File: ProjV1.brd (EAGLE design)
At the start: 94.9 x 63.5 mm, 24 parts, among them IC1 CD4007UBM, IC2 CD4007UBM, IC3 CD4007UBM, SW1 EC12E_SW, U1 MIC5504-3.3YM5-T5, U2 MCP2200-I/SS, U3 ATMEGA328PB-AU, Y1 12MHz

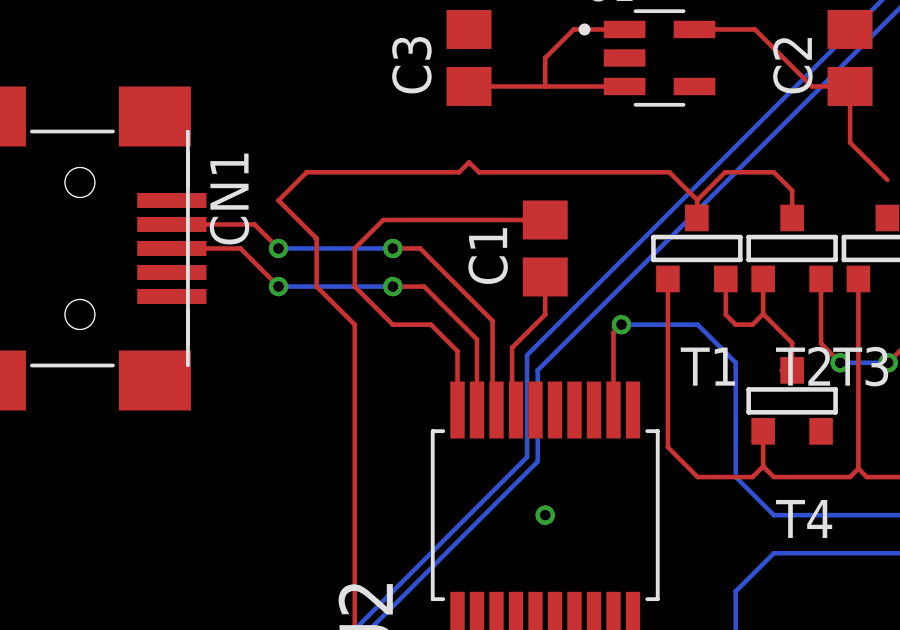
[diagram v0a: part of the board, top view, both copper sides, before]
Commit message: Updated schematic and pdf
Switched serial chip to run on 3.3V and  updated the pdf file
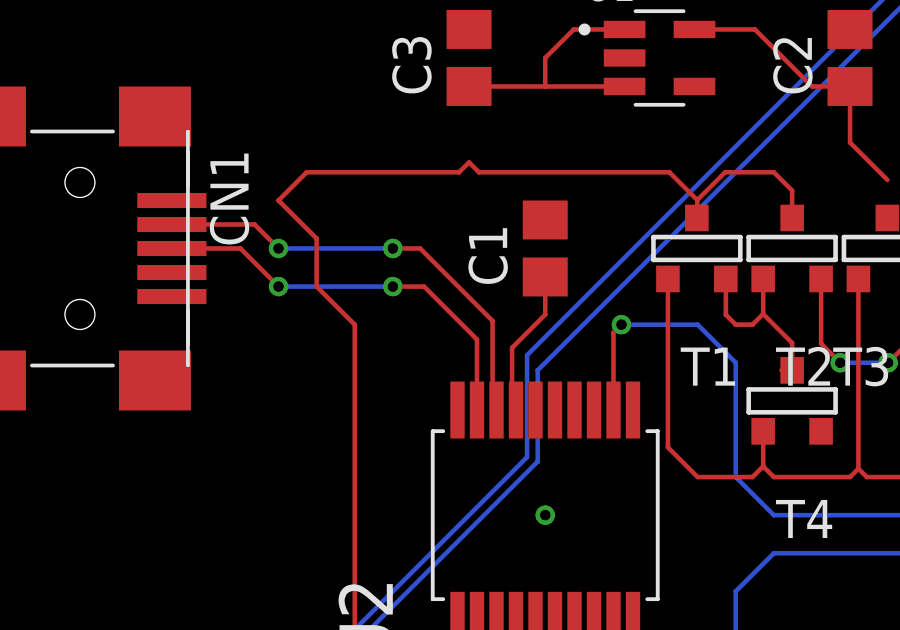
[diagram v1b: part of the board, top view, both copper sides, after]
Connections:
- removed net N$11: C1.2, U2.20
- removed net N$21: C1.1, U2.17
- new net VSS: U2.20
- net +5V: no longer U2.1
- net 0: now also C1.2
- net VCC: now also C1.1, U2.1, U2.17
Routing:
- net N$11: track 15.0 -> 0.00 mm
- net VCC: track 46.7 -> 51.6 mm
- net N$21: track 4.95 -> 0.00 mm
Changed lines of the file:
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@@
 <contactref element="IC3" pad="9"/>
 <contactref element="IC2" pad="9"/>
+<contactref element="C1" pad="2"/>
 <wire x1="49.16" y1="74.53" x2="57.52" y2="75.33" width="0" layer="19" extent="1-1"/>
 <wire x1="35.4847" y1="78.4235" x2="49.16" y2="74.53" width="0" layer="19" extent="1-1"/>
@@
 <wire x1="21.695" y1="78.74" x2="29.21" y2="79.69" width="0" layer="19" extent="1-1"/>
 <wire x1="16.51" y1="79.69" x2="21.695" y2="78.74" width="0" layer="19" extent="1-1"/>
-<wire x1="6.604" y1="70.79" x2="16.51" y2="79.69" width="0" layer="19" extent="1-1"/>
-<wire x1="28.2448" y1="66.294" x2="29.21" y2="79.69" width="0" layer="19" extent="1-1"/>
+<wire x1="19.05" y1="73.34" x2="21.695" y2="78.74" width="0" layer="19" extent="1-1"/>
+<wire x1="28.2448" y1="66.294" x2="19.05" y2="73.34" width="0" layer="19" extent="1-1"/>
+<wire x1="6.604" y1="70.79" x2="19.05" y2="73.34" width="0" layer="19" extent="1-1"/>
 <wire x1="17.78" y1="54.61" x2="28.2448" y2="66.294" width="0" layer="19" extent="1-1"/>
 <wire x1="29.21" y1="41.738" x2="17.78" y2="54.61" width="0" layer="19" extent="1-1"/>
@@
 <wire x1="59.69" y1="47.162" x2="60.96" y2="41.738" width="0" layer="19" extent="1-1"/>
 <wire x1="81.28" y1="33.43" x2="60.96" y2="41.738" width="0" layer="19" extent="1-1"/>
-</signal>
-<signal name="N$21">
-<contactref element="U2" pad="17"/>
-<contactref element="C1" pad="1"/>
-<wire x1="19.05" y1="71.44" x2="19.05" y2="70.18513125" width="0.1524" layer="1"/>
-<wire x1="17.9444" y1="69.07953125" x2="19.05" y2="70.18513125" width="0.1524" layer="1"/>
-<wire x1="18.075" y1="67.005" x2="17.9444" y2="67.1356" width="0.1524" layer="1"/>
-<wire x1="17.9444" y1="67.1356" x2="17.9444" y2="69.07953125" width="0.1524" layer="1"/>
 </signal>
 <signal name="VCC">
@@
 <contactref element="U3" pad="18"/>
 <contactref element="U$1" pad="2"/>
+<contactref element="U2" pad="1"/>
+<contactref element="U2" pad="17"/>
+<contactref element="C1" pad="1"/>
+<wire x1="19.05" y1="71.44" x2="19.05" y2="70.18513125" width="0.1524" layer="1"/>
+<wire x1="17.9444" y1="69.07953125" x2="19.05" y2="70.18513125" width="0.1524" layer="1"/>
+<wire x1="18.075" y1="67.005" x2="17.9444" y2="67.1356" width="0.1524" layer="1"/>
+<wire x1="17.9444" y1="67.1356" x2="17.9444" y2="69.07953125" width="0.1524" layer="1"/>
 <wire x1="40.64" y1="76.2" x2="49.16" y2="76.93" width="0" layer="19" extent="1-1"/>
 <wire x1="30.4546" y1="74.676" x2="40.64" y2="76.2" width="0" layer="19" extent="1-1"/>
 <wire x1="30.4546" y1="73.406" x2="30.4546" y2="74.676" width="0" layer="19" extent="1-1"/>
+<wire x1="19.05" y1="71.44" x2="24.025" y2="79.69" width="0" layer="19" extent="1-1"/>
+<wire x1="16.125" y1="59.995" x2="18.075" y2="67.005" width="0" layer="19" extent="1-1"/>
 <wire x1="78.74" y1="33.43" x2="62.23" y2="73.66" width="0" layer="19" extent="1-1"/>
 </signal>
@@
 <wire x1="2.4213" y1="45.4388" x2="16.9213" y2="42.9388" width="0" layer="19" extent="1-1"/>
 </signal>
-<signal name="N$11">
-<contactref element="U2" pad="20"/>
-<contactref element="C1" pad="2"/>
-<wire x1="19.05" y1="73.34" x2="13.65" y2="73.34" width="0.1524" layer="1"/>
-<wire x1="13.65" y1="73.34" x2="12.7" y2="72.39" width="0.1524" layer="1"/>
-<wire x1="16.125" y1="67.005" x2="16.125" y2="67.695" width="0.1524" layer="1"/>
-<wire x1="12.7" y1="72.39" x2="12.7" y2="71.12" width="0.1524" layer="1"/>
-<wire x1="12.7" y1="71.12" x2="13.97" y2="69.85" width="0.1524" layer="1"/>
-<wire x1="15.24" y1="69.85" x2="13.97" y2="69.85" width="0.1524" layer="1"/>
-<wire x1="16.125" y1="67.005" x2="16.125" y2="68.965" width="0.1524" layer="1"/>
-<wire x1="16.125" y1="68.965" x2="15.24" y2="69.85" width="0.1524" layer="1"/>
-</signal>
 <signal name="N$30">
 <contactref element="U3" pad="20"/>
@@
 <wire x1="20" y1="79.69" x2="19.05" y2="78.74" width="0.1524" layer="1"/>
 <wire x1="19.05" y1="78.74" x2="19.05" y2="77.79" width="0.1524" layer="1"/>
-<contactref element="U2" pad="1"/>
 <contactref element="T1" pad="1"/>
 <contactref element="T2" pad="1"/>
@@
 <wire x1="11.43" y1="71.12" x2="11.43" y2="72.72" width="0.1524" layer="1"/>
 <wire x1="24.1046" y1="73.406" x2="21.695" y2="77.79" width="0" layer="19" extent="1-1"/>
-<wire x1="16.125" y1="59.995" x2="16.125" y2="58.035" width="0" layer="19" extent="1-1"/>
 <wire x1="6.604" y1="73.99" x2="16.51" y2="77.79" width="0" layer="19" extent="1-1"/>
 </signal>
+<signal name="VSS">
+<contactref element="U2" pad="20"/>
+</signal>
 </signals>

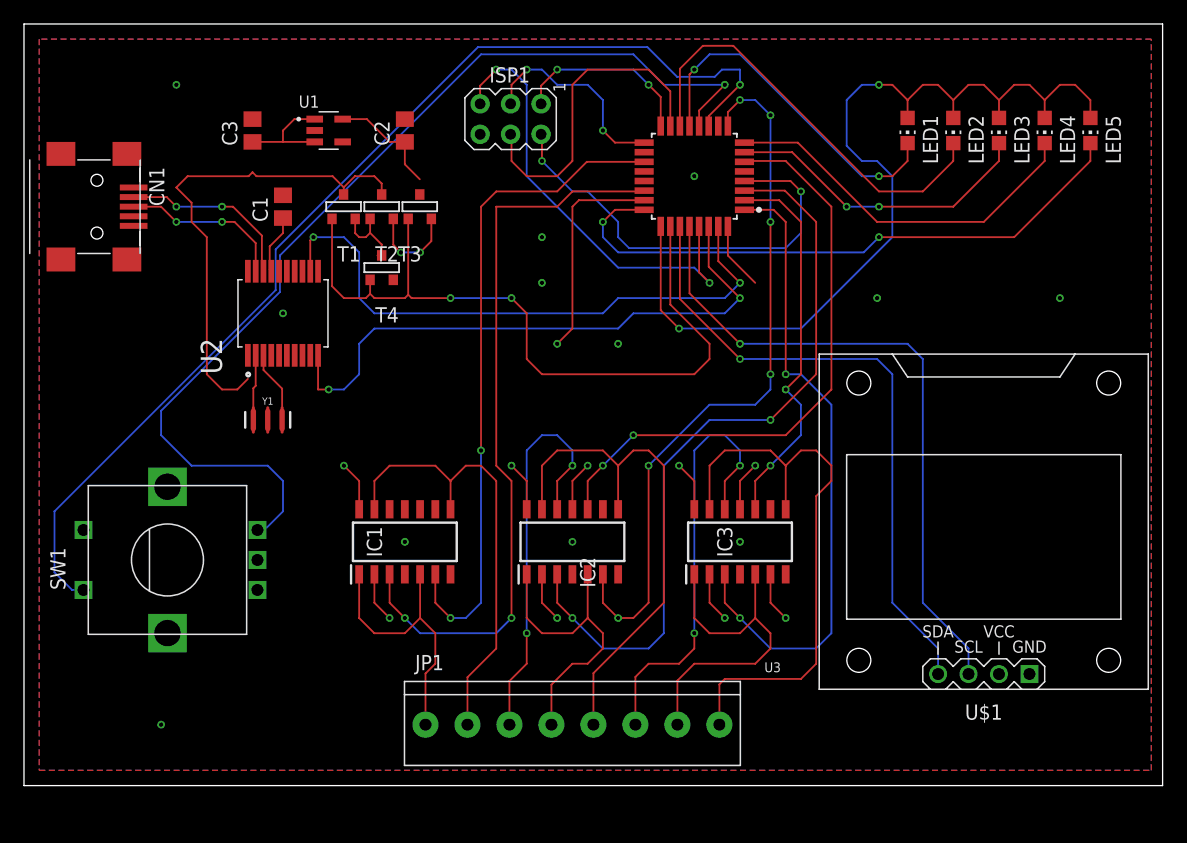
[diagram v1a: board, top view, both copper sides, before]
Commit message: Updated Board Layout and Cam filse
Rerouted wires to make board smaller
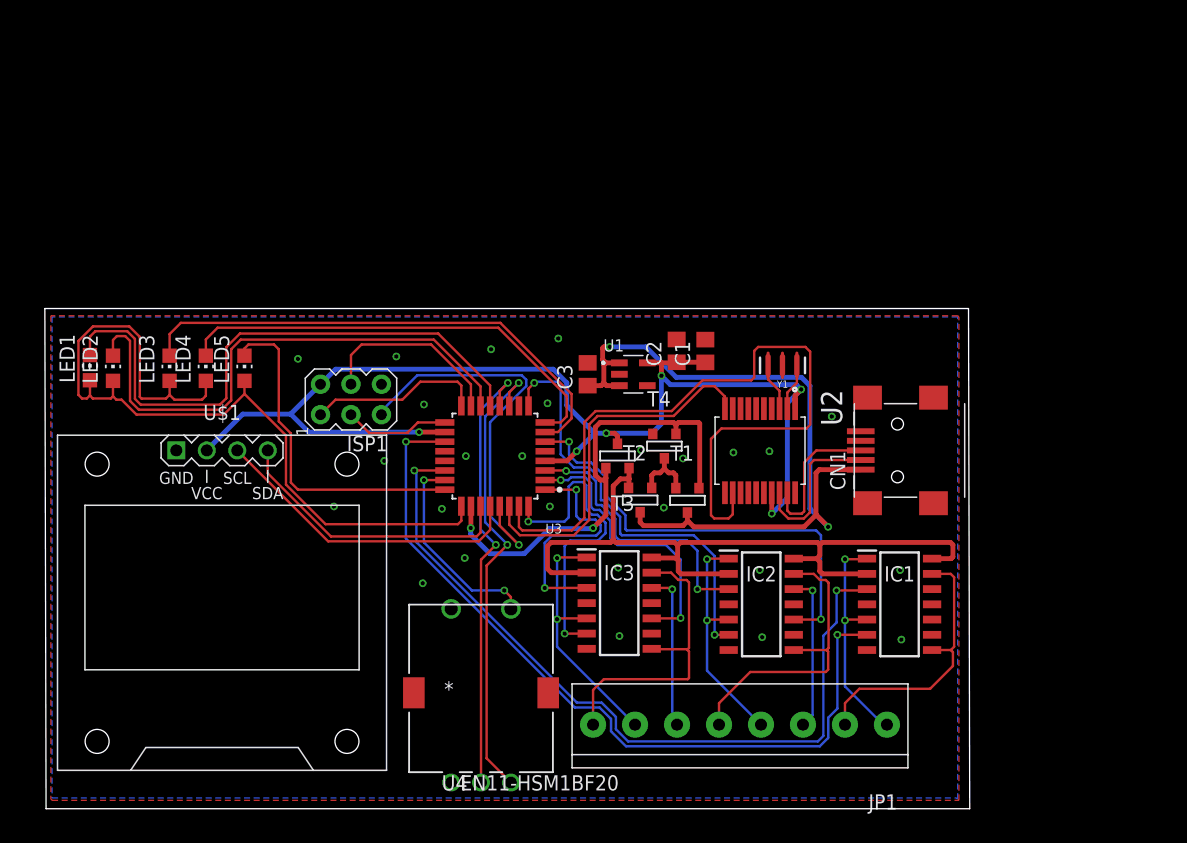
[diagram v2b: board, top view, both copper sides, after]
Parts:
- removed SW1: EC12E_SW, switch-alps:ALPS_EC12E_SW
- added U4: EN11-HSM1BF20, EN11-HSM1BF20:EN11-HSM_TTE
- moved LED5 73.3 mm to (15.8, 58.9), turned to 0 degrees
- moved LED2 72.8 mm to (4.88, 58.9), turned to 0 degrees
- moved LED4 72.7 mm to (12.6, 58.9), turned to 0 degrees
- moved LED3 71.9 mm to (9.60, 58.9), turned to 0 degrees
- moved CN1 71.7 mm to (71.3, 52.1), turned to 90 degrees
- moved LED1 71.0 mm to (2.96, 59.0), turned to 0 degrees
- moved U$1 63.9 mm to (14.0, 39.4), turned to 0 degrees
- moved Y1 43.2 mm to (60.7, 59.2), turned to 180 degrees
- moved IC1 41.6 mm to (70.5, 39.2), turned to 0 degrees
- moved U2 41.4 mm to (58.8, 52.0), turned to 270 degrees
- moved T1 37.7 mm to (52.7, 47.9), turned to 0 degrees
- moved C1 37.2 mm to (54.3, 60.4)
- moved C3 34.5 mm to (44.5, 58.4)
- moved T2 32.6 mm to (48.8, 47.9), turned to 0 degrees
- moved U1 32.5 mm to (48.3, 58.4)
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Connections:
- removed net N$7: SW1.C, SW1.E
- net 0: now also U4.1, U4.4
- net CLK: now also U4.3; no longer SW1.B
- net DT: now also U4.5; no longer SW1.A
- net SW: now also U4.2; no longer SW1.D
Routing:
- net SW: track 90.4 -> 39.0 mm, vias 1 -> 2
- net VCC: track 51.6 -> 101.6 mm, vias 2 -> 6
- net CLK: track 85.5 -> 37.5 mm, vias 1 -> 2
- net LC5: track 62.9 -> 23.2 mm
- net LC2: track 53.8 -> 20.0 mm
- net SDA: track 52.9 -> 24.2 mm, vias 1 -> 0
- net SCL: track 55.1 -> 26.6 mm, vias 1 -> 0
- net LC: track 41.3 -> 66.8 mm, vias 10 -> 0
- net LC4: track 60.0 -> 36.2 mm, vias 6 -> 2
- net C3: track 36.7 -> 13.2 mm, vias 2 -> 1
- net VSET: track 63.3 -> 39.9 mm
- net C1: track 48.7 -> 25.8 mm
- net LED5: track 50.9 -> 28.4 mm, vias 2 -> 0
- net C6: track 33.8 -> 13.1 mm, vias 2 -> 1
- net LED1: track 29.4 -> 49.0 mm, vias 2 -> 0
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- added copper zone on layer 1, net 0
- added copper zone on layer 16, net 0
- removed copper zone on layer 1, net GND
- removed copper zone on layer 16, net GND
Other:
- board size 94.9 x 63.5 mm -> 77.1 x 41.7 mm
